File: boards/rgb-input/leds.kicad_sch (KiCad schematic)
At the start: 0 parts

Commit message: figured out most of the components, working on placement
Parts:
- added J46: RGB, Connector_IDC:IDC-Header_2x25_P2.54mm_Vertical, symbol Connector_Generic:Conn_02x25_Odd_Even
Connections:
- new net +5V: J46.1 (Pin_1)
- new net BLUE0: J46.5 (Pin_5)
- new net BLUE1: J46.8 (Pin_8)
- new net BLUE10: J46.35 (Pin_35)
- new net BLUE11: J46.38 (Pin_38)
- new net BLUE12: J46.41 (Pin_41)
- new net BLUE13: J46.44 (Pin_44)
- new net BLUE14: J46.47 (Pin_47)
- new net BLUE15: J46.50 (Pin_50)
- new net BLUE2: J46.11 (Pin_11)
- new net BLUE3: J46.14 (Pin_14)
- new net BLUE4: J46.17 (Pin_17)
- new net BLUE5: J46.20 (Pin_20)
- new net BLUE6: J46.23 (Pin_23)
- new net BLUE7: J46.26 (Pin_26)
- new net BLUE8: J46.29 (Pin_29)
- new net BLUE9: J46.32 (Pin_32)
- new net GNDD: J46.2 (Pin_2)
- new net GREEN0: J46.4 (Pin_4)
- new net GREEN1: J46.7 (Pin_7)
- new net GREEN10: J46.34 (Pin_34)
- new net GREEN11: J46.37 (Pin_37)
- new net GREEN12: J46.40 (Pin_40)
- new net GREEN13: J46.43 (Pin_43)
- new net GREEN14: J46.46 (Pin_46)
- new net GREEN15: J46.49 (Pin_49)
- new net GREEN2: J46.10 (Pin_10)
- new net GREEN3: J46.13 (Pin_13)
- new net GREEN4: J46.16 (Pin_16)
- new net GREEN5: J46.19 (Pin_19)
- new net GREEN6: J46.22 (Pin_22)
- new net GREEN7: J46.25 (Pin_25)
- new net GREEN8: J46.28 (Pin_28)
- new net GREEN9: J46.31 (Pin_31)
- new net RED0: J46.3 (Pin_3)
- new net RED1: J46.6 (Pin_6)
- new net RED10: J46.33 (Pin_33)
- new net RED11: J46.36 (Pin_36)
- new net RED12: J46.39 (Pin_39)
- new net RED13: J46.42 (Pin_42)
- new net RED14: J46.45 (Pin_45)
- new net RED15: J46.48 (Pin_48)
- new net RED2: J46.9 (Pin_9)
- new net RED3: J46.12 (Pin_12)
- new net RED4: J46.15 (Pin_15)
- new net RED5: J46.18 (Pin_18)
- new net RED6: J46.21 (Pin_21)
- new net RED7: J46.24 (Pin_24)
- new net RED8: J46.27 (Pin_27)
- new net RED9: J46.30 (Pin_30)

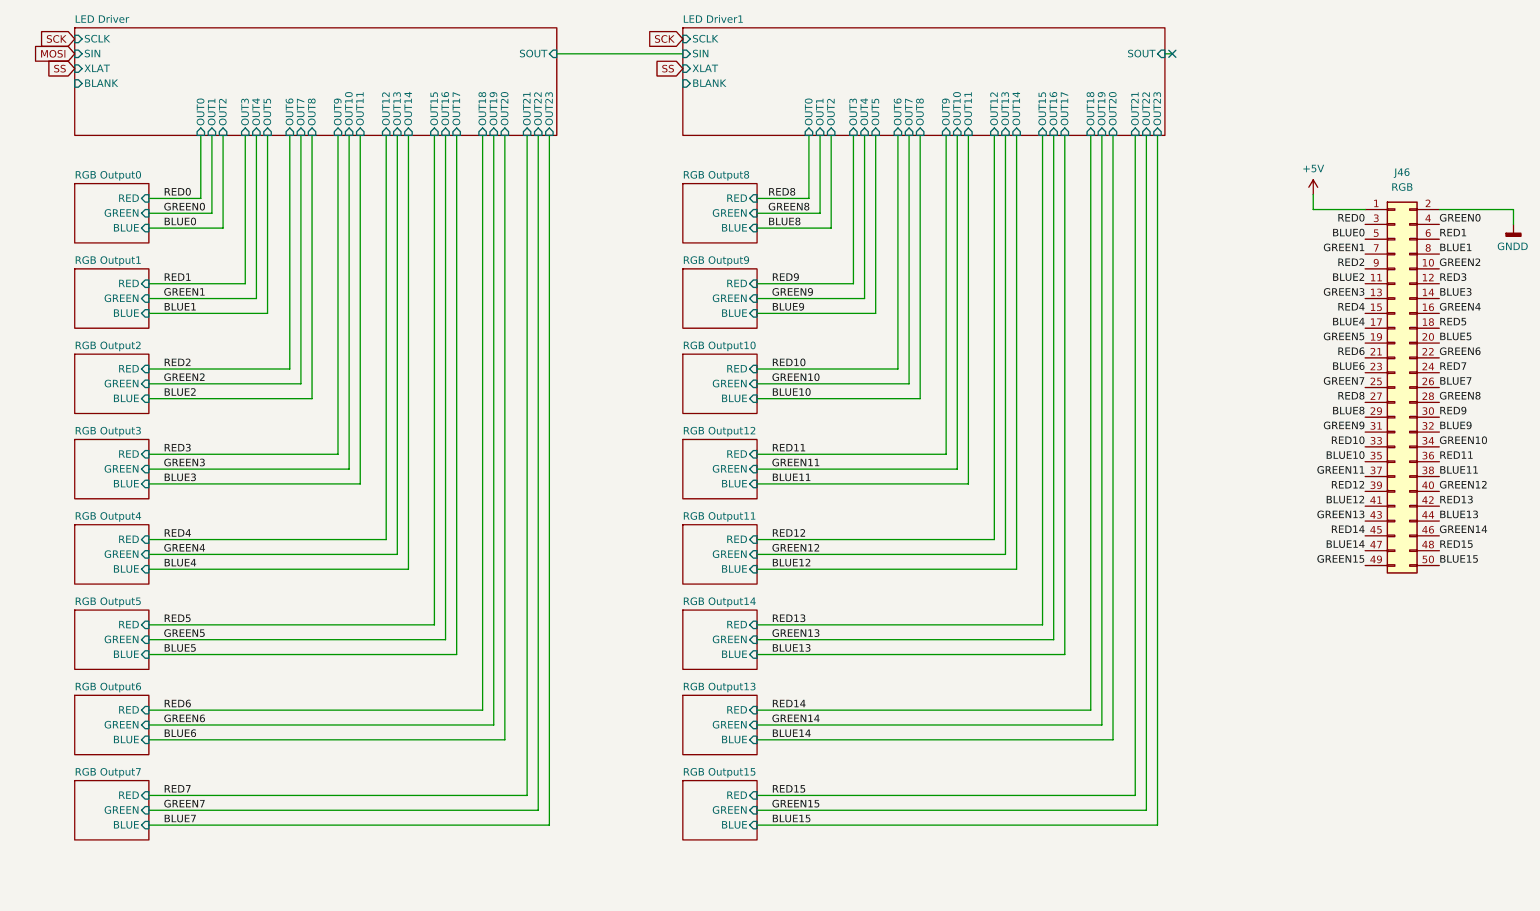
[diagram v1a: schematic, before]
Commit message: routed the rgb setup
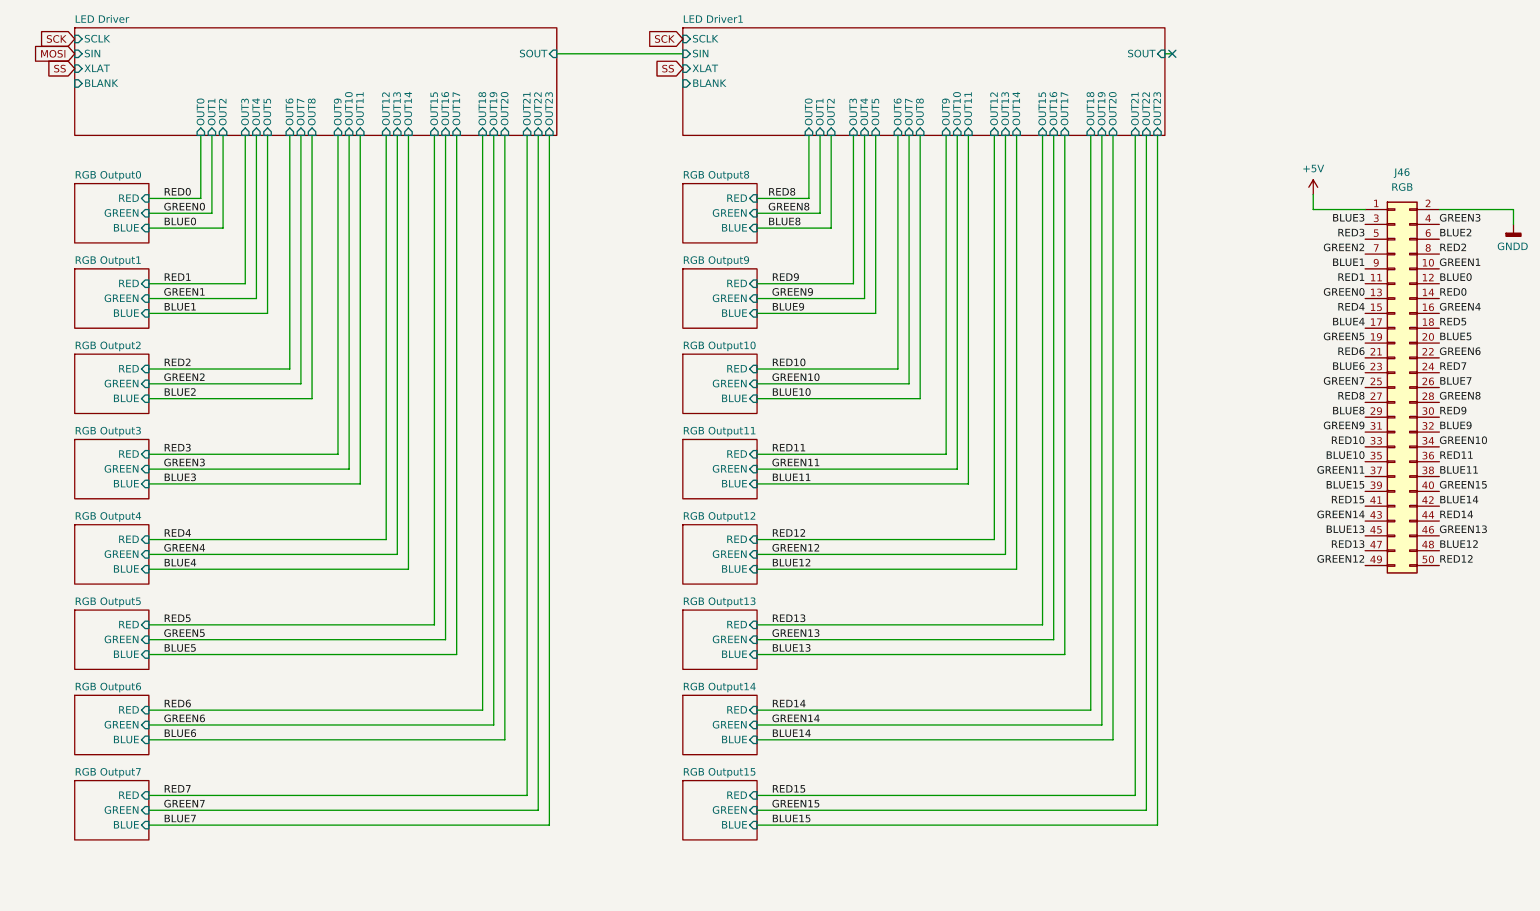
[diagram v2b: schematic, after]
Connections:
- net BLUE0: now also J46.12 (Pin_12); no longer J46.5 (Pin_5)
- net BLUE1: now also J46.9 (Pin_9); no longer J46.8 (Pin_8)
- net BLUE12: now also J46.48 (Pin_48); no longer J46.41 (Pin_41)
- net BLUE13: now also J46.45 (Pin_45); no longer J46.44 (Pin_44)
- net BLUE14: now also J46.42 (Pin_42); no longer J46.47 (Pin_47)
- net BLUE15: now also J46.39 (Pin_39); no longer J46.50 (Pin_50)
- net BLUE2: now also J46.6 (Pin_6); no longer J46.11 (Pin_11)
- net BLUE3: now also J46.3 (Pin_3); no longer J46.14 (Pin_14)
- net GREEN0: now also J46.13 (Pin_13); no longer J46.4 (Pin_4)
- net GREEN1: now also J46.10 (Pin_10); no longer J46.7 (Pin_7)
- net GREEN12: now also J46.49 (Pin_49); no longer J46.40 (Pin_40)
- net GREEN13: now also J46.46 (Pin_46); no longer J46.43 (Pin_43)
- net GREEN14: now also J46.43 (Pin_43); no longer J46.46 (Pin_46)
- net GREEN15: now also J46.40 (Pin_40); no longer J46.49 (Pin_49)
- net GREEN2: now also J46.7 (Pin_7); no longer J46.10 (Pin_10)
- net GREEN3: now also J46.4 (Pin_4); no longer J46.13 (Pin_13)
- net RED0: now also J46.14 (Pin_14); no longer J46.3 (Pin_3)
- net RED1: now also J46.11 (Pin_11); no longer J46.6 (Pin_6)
- net RED12: now also J46.50 (Pin_50); no longer J46.39 (Pin_39)
- net RED13: now also J46.47 (Pin_47); no longer J46.42 (Pin_42)
- net RED14: now also J46.44 (Pin_44); no longer J46.45 (Pin_45)
- net RED15: now also J46.41 (Pin_41); no longer J46.48 (Pin_48)
- net RED2: now also J46.8 (Pin_8); no longer J46.9 (Pin_9)
- net RED3: now also J46.5 (Pin_5); no longer J46.12 (Pin_12)

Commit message: so much routing.
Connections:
- no-connect marks 1 -> 3
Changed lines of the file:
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@@
 (kicad_sch (version 20230121) (generator eeschema)
   (paper "A4")
+  (no_connect (at 124.46 29.21))
+  (no_connect (at 20.32 29.21))
   (no_connect (at 210.82 24.13))
   (wire (pts (xy 175.895 97.79) (xy 175.895 38.1))
@@
     (stroke (width 0) (type default))
   )
+  (wire (pts (xy 20.32 29.21) (xy 22.86 29.21))
+    (stroke (width 0) (type default))
+  )
   (wire (pts (xy 182.245 109.855) (xy 139.7 109.855))
     (stroke (width 0) (type default))
@@
     (stroke (width 0) (type default))
   )
+  (wire (pts (xy 124.46 29.21) (xy 127 29.21))
+    (stroke (width 0) (type default))
+  )

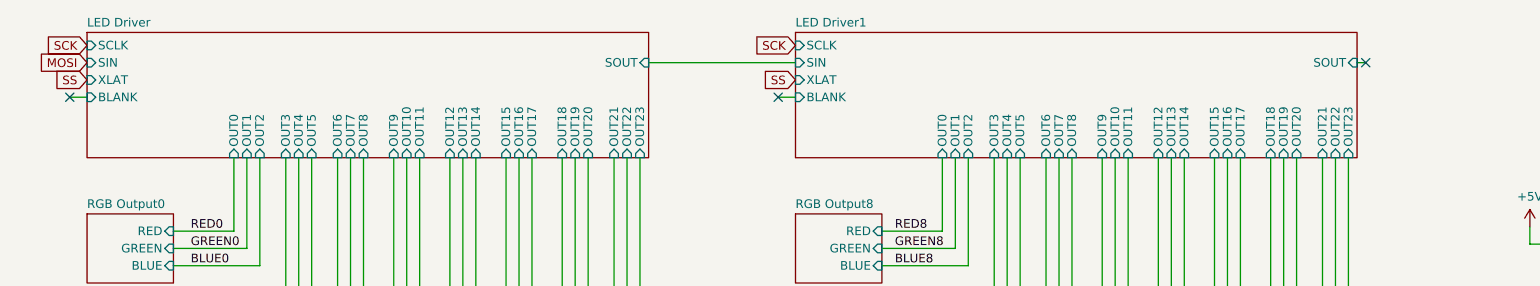
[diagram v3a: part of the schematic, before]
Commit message: whoa, board is fully routed!!!!
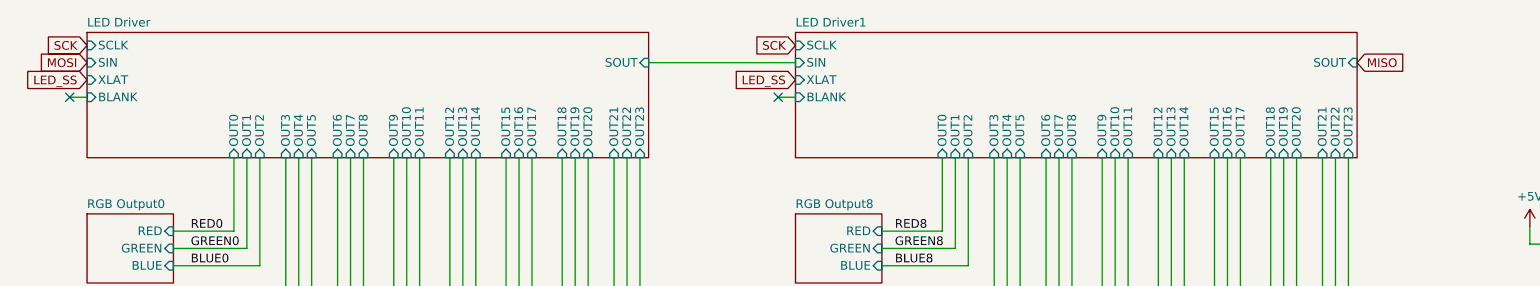
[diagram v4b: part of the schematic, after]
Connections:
- no-connect marks 3 -> 2
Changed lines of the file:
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@@
   (no_connect (at 124.46 29.21))
   (no_connect (at 20.32 29.21))
-  (no_connect (at 210.82 24.13))
   (wire (pts (xy 175.895 97.79) (xy 175.895 38.1))
     (stroke (width 0) (type default))
@@
     (stroke (width 0) (type default))
   )
-  (wire (pts (xy 209.55 24.13) (xy 210.82 24.13))
-    (stroke (width 0) (type default))
-  )
   (wire (pts (xy 172.085 92.71) (xy 172.085 38.1))
     (stroke (width 0) (type default))
@@
     (effects (font (size 1.27 1.27)) (justify left bottom))
   )
-  (global_label "SS" (shape input) (at 22.86 26.67 180) (fields_autoplaced)
+  (global_label "LED_SS" (shape input) (at 22.86 26.67 180) (fields_autoplaced)
     (effects (font (size 1.27 1.27)) (justify right))
-    (property "Intersheetrefs" "${INTERSHEET_REFS}" (at 17.4558 26.67 0)
+    (property "Intersheetrefs" "${INTERSHEET_REFS}" (at 13.0411 26.67 0)
       (effects (font (size 1.27 1.27)) (justify right) hide)
     )
@@
     )
   )
+  (global_label "LED_SS" (shape input) (at 127 26.67 180) (fields_autoplaced)
+    (effects (font (size 1.27 1.27)) (justify right))
+    (property "Intersheetrefs" "${INTERSHEET_REFS}" (at 117.1811 26.67 0)
+      (effects (font (size 1.27 1.27)) (justify right) hide)
+    )
+  )
   (global_label "MOSI" (shape input) (at 22.86 24.13 180) (fields_autoplaced)
     (effects (font (size 1.27 1.27)) (justify right))
@@
     )
   )
-  (global_label "SS" (shape input) (at 127 26.67 180) (fields_autoplaced)
-    (effects (font (size 1.27 1.27)) (justify right))
-    (property "Intersheetrefs" "${INTERSHEET_REFS}" (at 121.5958 26.67 0)
-      (effects (font (size 1.27 1.27)) (justify right) hide)
+  (global_label "MISO" (shape input) (at 209.55 24.13 0) (fields_autoplaced)
+    (effects (font (size 1.27 1.27)) (justify left))
+    (property "Intersheetrefs" "${INTERSHEET_REFS}" (at 217.1314 24.13 0)
+      (effects (font (size 1.27 1.27)) (justify left) hide)
     )
   )

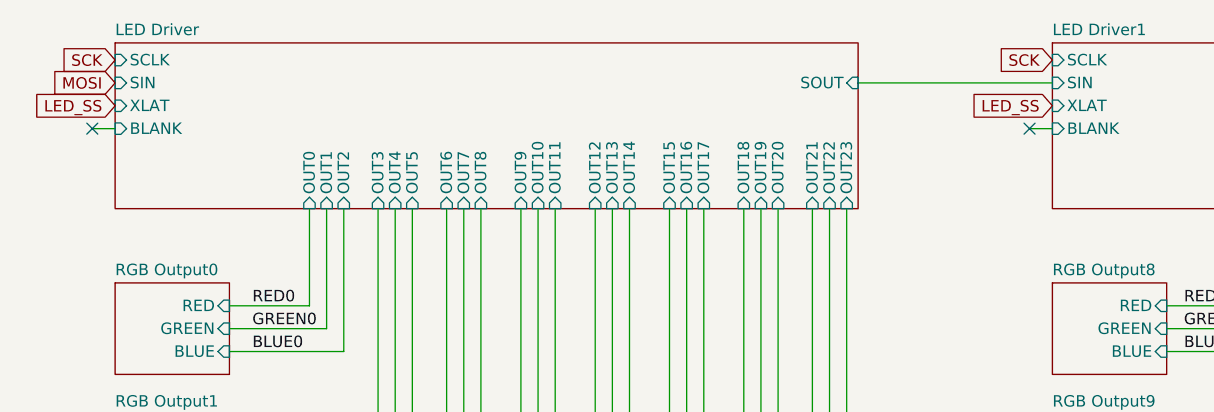
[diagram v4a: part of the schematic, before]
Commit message: added 5v fuse to schematic
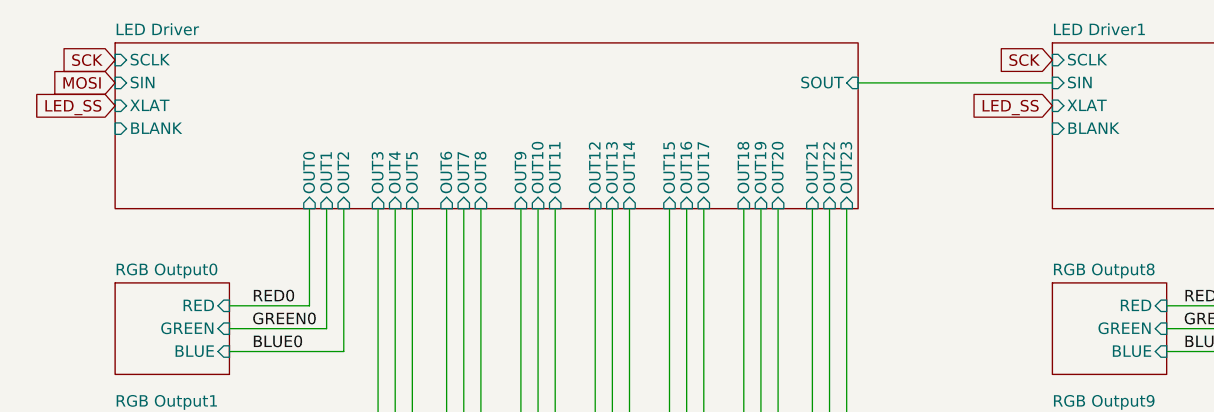
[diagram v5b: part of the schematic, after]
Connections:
- no-connect marks 2 -> 0
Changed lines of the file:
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@@
 (kicad_sch (version 20230121) (generator eeschema)
   (paper "A4")
-  (no_connect (at 124.46 29.21))
-  (no_connect (at 20.32 29.21))
   (wire (pts (xy 175.895 97.79) (xy 175.895 38.1))
     (stroke (width 0) (type default))
@@
     (stroke (width 0) (type default))
   )
-  (wire (pts (xy 20.32 29.21) (xy 22.86 29.21))
-    (stroke (width 0) (type default))
-  )
   (wire (pts (xy 182.245 109.855) (xy 139.7 109.855))
     (stroke (width 0) (type default))
@@
     (stroke (width 0) (type default))
   )
-  (wire (pts (xy 124.46 29.21) (xy 127 29.21))
-    (stroke (width 0) (type default))
-  )

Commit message: more BOM updates.
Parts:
- J46: LCSC (none) -> C30006
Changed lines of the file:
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@@
+      (effects (font (size 1.27 1.27)) hide)
+    )
+    (property "LCSC" "C30006" (at 248.92 81.28 0)
       (effects (font (size 1.27 1.27)) hide)
     )

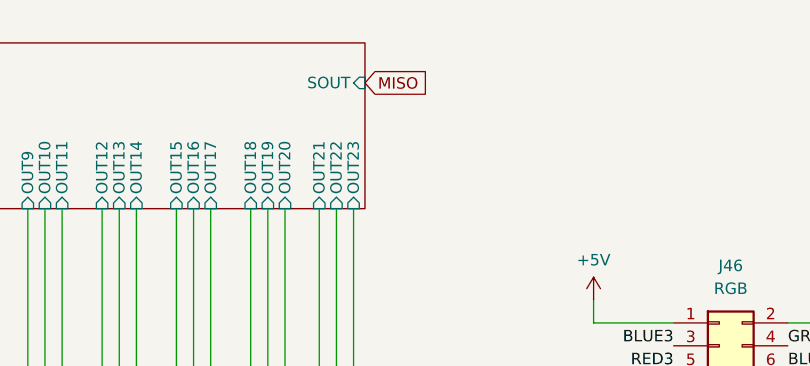
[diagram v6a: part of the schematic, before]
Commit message: solved the ADC issue and found another minor one
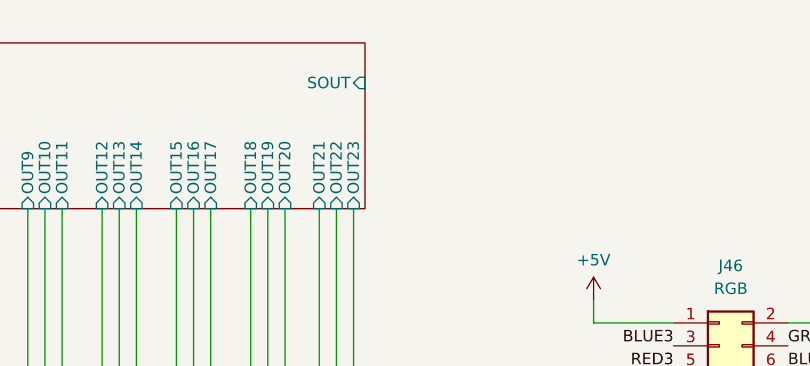
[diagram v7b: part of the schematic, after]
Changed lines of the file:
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@@
-    )
-  )
-  (global_label "MISO" (shape input) (at 209.55 24.13 0) (fields_autoplaced)
-    (effects (font (size 1.27 1.27)) (justify left))
-    (property "Intersheetrefs" "${INTERSHEET_REFS}" (at 217.1314 24.13 0)
-      (effects (font (size 1.27 1.27)) (justify left) hide)
     )
   )
